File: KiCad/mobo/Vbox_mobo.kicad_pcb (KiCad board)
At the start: 2 copper layers, 33.1 x 114.3 mm, 46 parts, among them J1 Conn_01x02, J10 Conn_01x01, J11 Conn_01x01, J12 Conn_01x02, J13 Conn_01x02, J14 Conn_01x02, J15 Conn_01x02, J2 JTAG_TC2030, J3 DuPont Connector, J4 Conn_01x06, J5 Conn_01x06, J6 Conn_01x10, J7 Conn_01x10, J8 Conn_01x01, J9 Conn_01x01, SW1 Boot, U1 XC6206, U2 X05A26H12G, U3 RP2040, U4 W25Q128JVS, Y1 12MHz

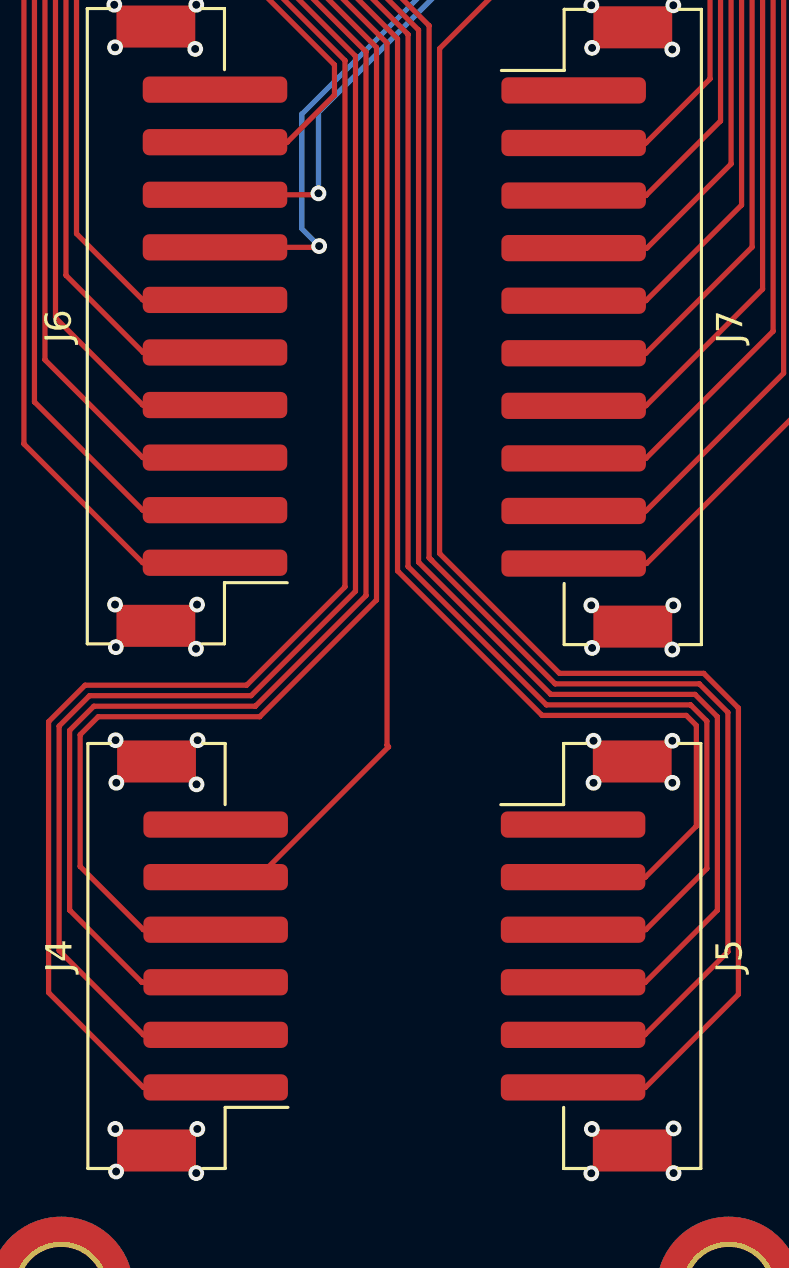
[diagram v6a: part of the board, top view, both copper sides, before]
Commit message: add labels to connectors on mobo
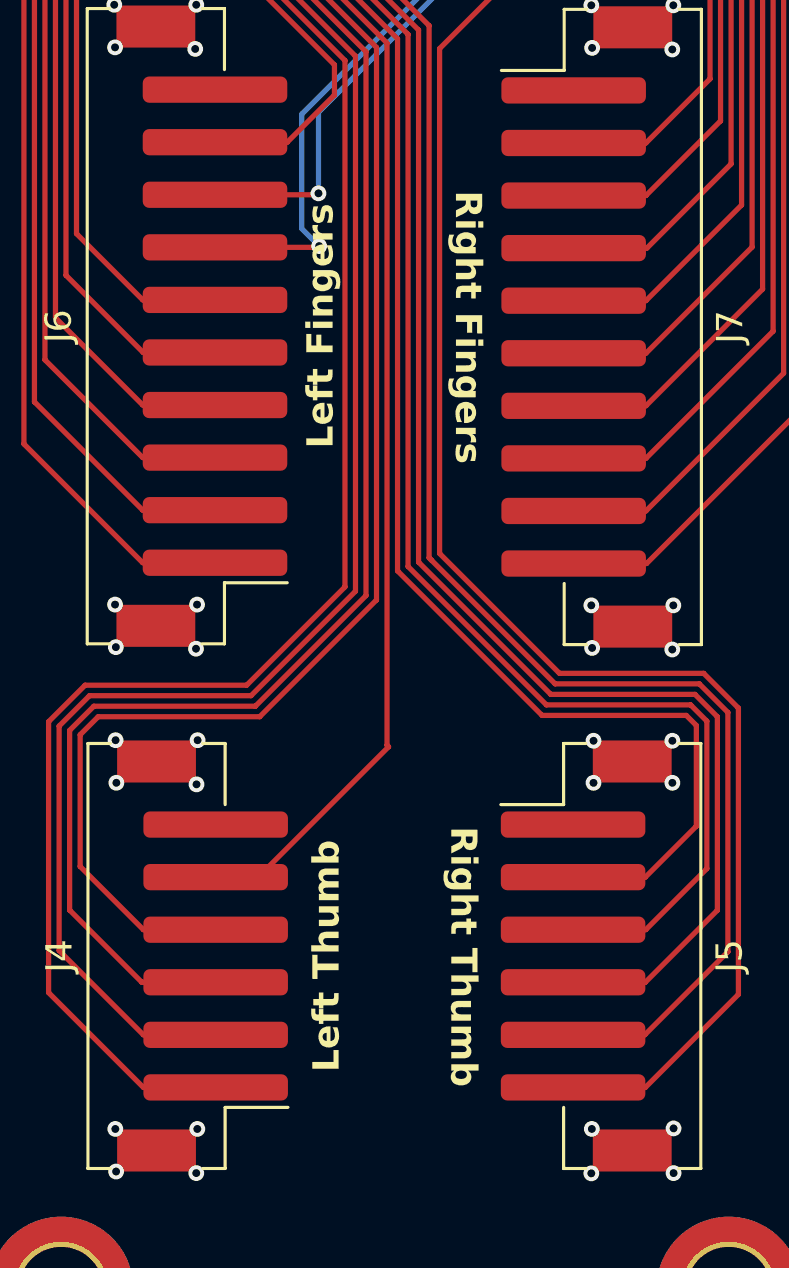
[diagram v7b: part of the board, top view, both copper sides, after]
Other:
- board text added: "Left Fingers"
- board text added: "Left Thumb"
- board text added: "Right Fingers"
- board text added: "Right Thumb"
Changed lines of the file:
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@@
     (effects (font (size 1 1) (thickness 0.2) bold) (justify left bottom mirror))
+  )
+  (gr_text "Right Thumb" (at 103.62 139.76 270) (layer "F.SilkS")
+    (effects (font (size 1 1) (thickness 0.2) bold) (justify bottom))
+  )
+  (gr_text "Left Fingers" (at 99.35 115.76 90) (layer "F.SilkS")
+    (effects (font (size 1 1) (thickness 0.2) bold) (justify bottom))
   )
   (gr_text "3.3V" (at 107.4 60.7) (layer "F.SilkS")
     (effects (font (size 1 1) (thickness 0.15)) (justify left bottom))
   )
+  (gr_text "Right Fingers" (at 103.8 115.81 270) (layer "F.SilkS")
+    (effects (font (size 1 1) (thickness 0.2) bold) (justify bottom))
+  )
+  (gr_text "Left Thumb" (at 99.58 139.73 90) (layer "F.SilkS")
+    (effects (font (size 1 1) (thickness 0.2) bold) (justify bottom))
+  )
   (gr_text "100nF" (at 94.882466 71.969019 180) (layer "F.Fab")

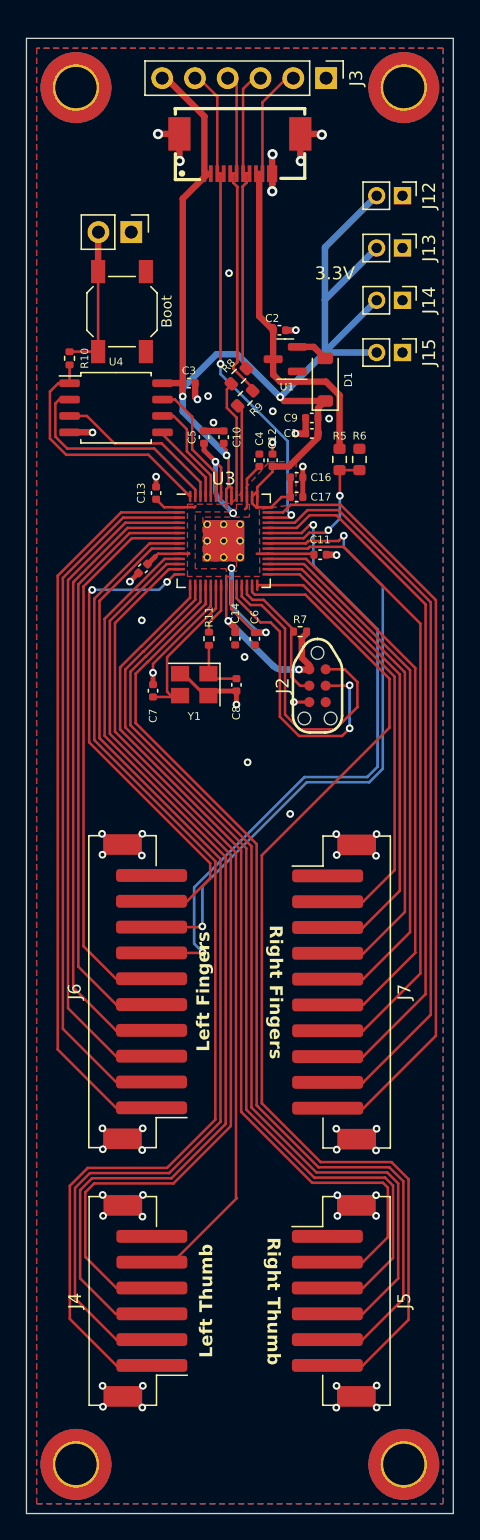
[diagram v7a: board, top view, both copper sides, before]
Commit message: flip connectors
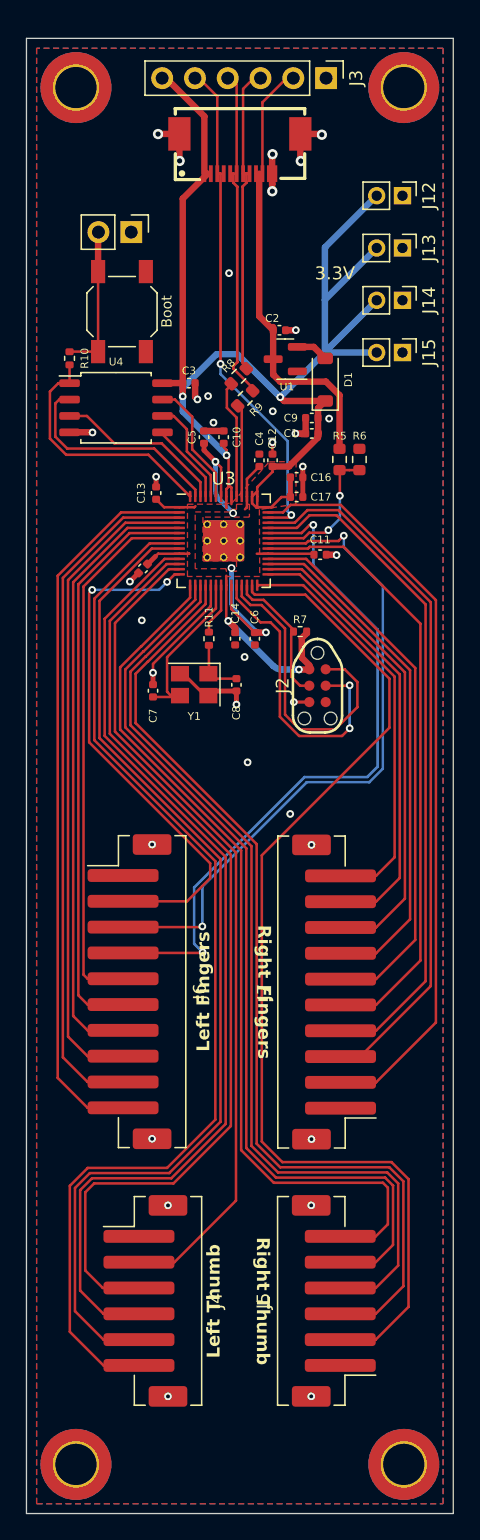
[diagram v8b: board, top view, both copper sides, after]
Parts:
- moved J6 1.20 mm to (93.0, 115.8), turned to -90 degrees
- turned J4 to -90 degrees
- turned J5 to 90 degrees
- turned J7 to 90 degrees
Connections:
- J4 pad 1: M1 -> GND
- J4 pad 2: M2 -> M5
- J4 pad 3: M3 -> M4
- J4 pad 4: M4 -> M3
- J4 pad 5: M5 -> M2
- J4 pad 6: GND -> M1
- J5 pad 2: C_UP -> C_RT
- J5 pad 3: C_LT -> C_DN
- J5 pad 5: C_DN -> C_LT
- J5 pad 6: C_RT -> C_UP
- J6 pad 1: START -> GND
- J6 pad 10: GND -> START
- J6 pad 2: UP2 -> INDEX2
- J6 pad 3: RIGHT -> RING2
- J6 pad 4: DOWN -> PINKY2
- J6 pad 5: LEFT -> L
- J6 pad 6: L -> LEFT
- J6 pad 7: PINKY2 -> DOWN
- J6 pad 8: RING2 -> RIGHT
- J6 pad 9: INDEX2 -> UP2
- J7 pad 10: RIGHTSTART -> UP
- J7 pad 2: UP -> RIGHTSTART
- J7 pad 3: MS -> R
- J7 pad 4: Z -> B
- J7 pad 5: LS -> Y
- J7 pad 7: Y -> LS
- J7 pad 8: B -> Z
- J7 pad 9: R -> MS
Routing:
- net R: track 58.1 -> 55.0 mm
- net Z: track 39.8 -> 37.4 mm
- net RIGHTSTART: track 60.8 -> 58.3 mm
- net LS: track 42.6 -> 40.2 mm
- net MS: track 37.0 -> 34.5 mm
- net Y: track 50.5 -> 48.0 mm
- net UP: track 34.9 -> 32.4 mm
- net X: track 45.4 -> 43.0 mm
- net B: track 55.3 -> 52.8 mm
- net M5: track 63.9 -> 64.8 mm
- net UP2: track 54.5 -> 53.6 mm
- net START: track 57.3 -> 56.4 mm
- net L: track 43.2 -> 42.2 mm
- net DOWN: track 48.8 -> 47.9 mm
- net RIGHT: track 51.6 -> 50.7 mm
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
